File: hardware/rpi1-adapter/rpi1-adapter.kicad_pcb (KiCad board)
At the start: 2 copper layers, 98 x 68 mm, 29 parts, among them P1 I2C, P2 CONN_02X13, P3 UART, P4 CONN_01X08, P5 relays, P6 12V, P7 CONN_01X08, P8 CONN_01X08, U1 OPTO-TRANSISTOR-4, U2 OPTO-TRANSISTOR-4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

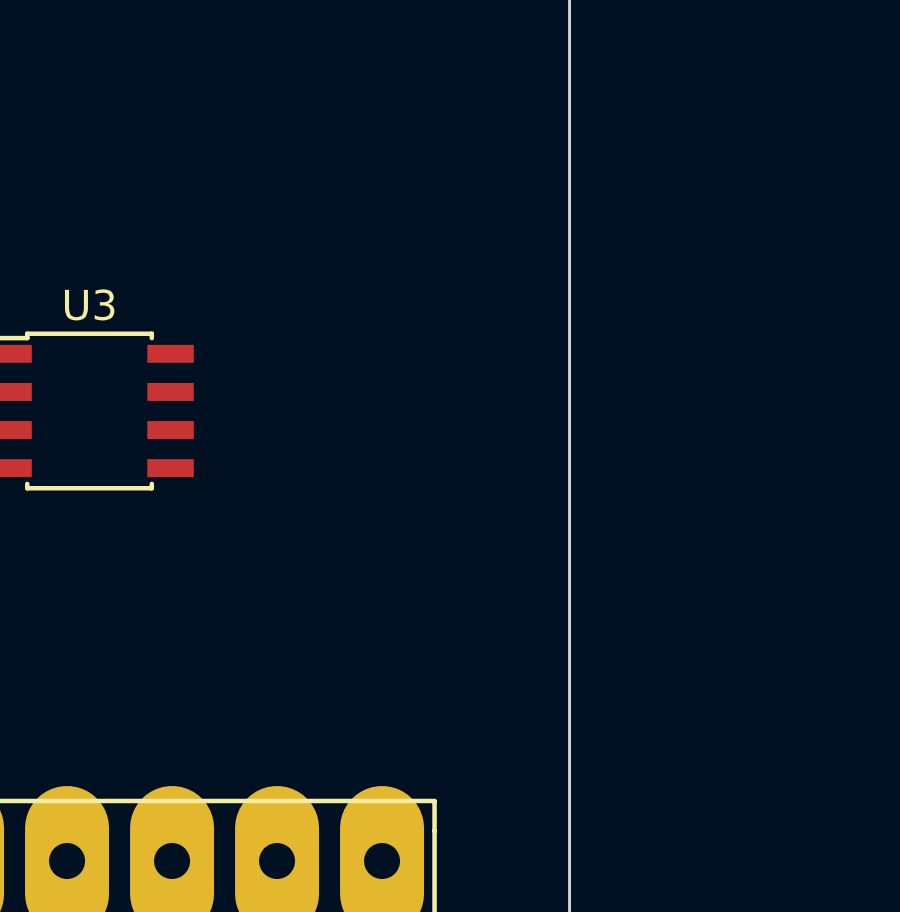
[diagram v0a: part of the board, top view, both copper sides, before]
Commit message: o Add dual P-mosfet to be used.
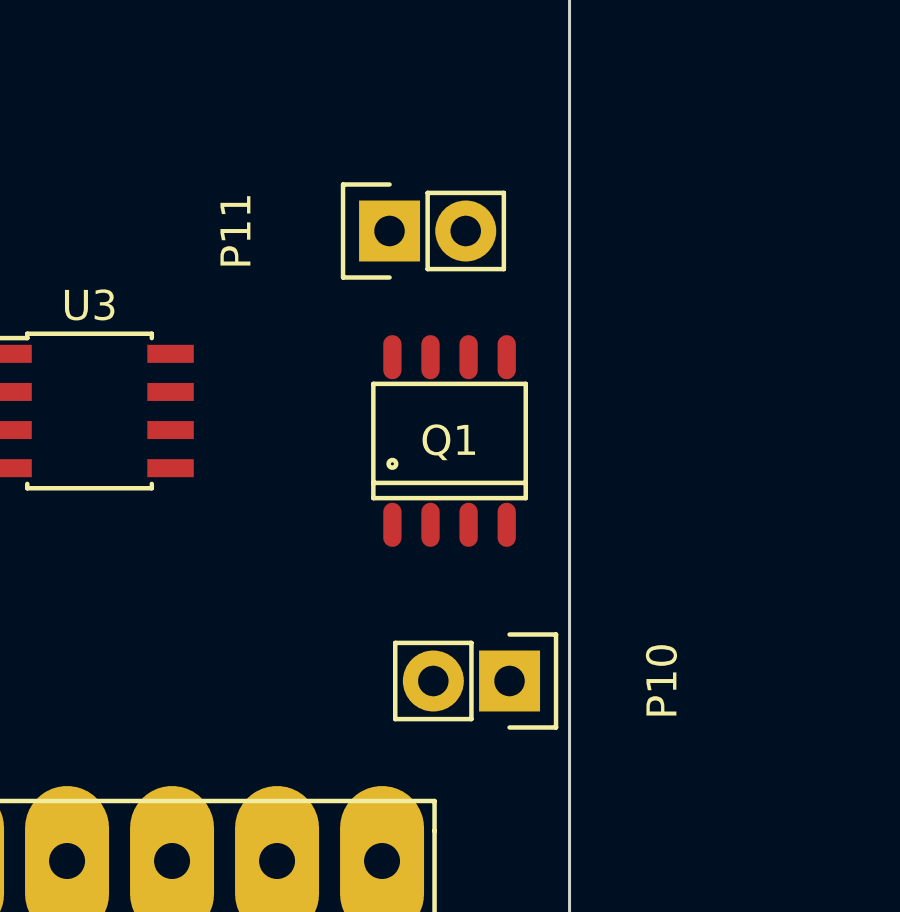
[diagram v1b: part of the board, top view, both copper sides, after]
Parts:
- added P10: CONN_01X02, Pin_Headers:Pin_Header_Straight_1x02, F.Cu at (146.0, 74.0)
- added P11: CONN_01X02, Pin_Headers:Pin_Header_Straight_1x02, F.Cu at (142.0, 59.0)
- added Q1: IRF9362PbF, SO-8, F.Cu at (144.0, 66.0)
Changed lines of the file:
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@@
 (kicad_pcb (version 4) (host pcbnew "(after 2015-may-25 BZR unknown)-product")
   (general
-    (links 96)
-    (no_connects 96)
-    (area 49.949999 21.949999 185.960003 90.050001)
+    (links 104)
+    (no_connects 104)
+    (area 49.949999 21.949999 148.050001 90.050001)
     (thickness 1.6)
     (drawings 4)
     (tracks 0)
     (zones 0)
-    (modules 29)
-    (nets 40)
+    (modules 32)
+    (nets 44)
   )
   (page A4)
@@
   (net 38 "Net-(C1-Pad1)")
   (net 39 "Net-(R10-Pad1)")
+  (net 40 "Net-(P11-Pad1)")
+  (net 41 "Net-(P10-Pad2)")
+  (net 42 "Net-(P11-Pad2)")
+  (net 43 "Net-(P10-Pad1)")
   (net_class Default "This is the default net class."
     (clearance 0.2)
@@
     (add_net "Net-(P1-Pad1)")
     (add_net "Net-(P1-Pad2)")
+    (add_net "Net-(P10-Pad1)")
+    (add_net "Net-(P10-Pad2)")
+    (add_net "Net-(P11-Pad1)")
+    (add_net "Net-(P11-Pad2)")
     (add_net "Net-(P2-Pad10)")
     (add_net "Net-(P2-Pad8)")
@@
     (pad 4 thru_hole oval (at -1.75 0) (size 2.8 5) (drill 1.2) (layers *.Cu *.Mask F.SilkS))
   )
+  (module SO-8 (layer F.Cu)
+    (at 144 66)
+    (descr "SO-8 Surface Mount Small Outline 150mil 8pin Package")
+    (tags "Power Integrations D Package")
+    (fp_text reference Q1 (at 0 0) (layer F.SilkS)
+      (effects (font (size 1 1) (thickness 0.15)))
+    )
+    (fp_text value IRF9362PbF (at 0 0) (layer F.Fab)
+      (effects (font (size 1 1) (thickness 0.15)))
+    )
+    (fp_circle (center -1.905 0.762) (end -1.778 0.762) (layer F.SilkS) (width 0.15))
+    (fp_line (start -2.54 1.397) (end 2.54 1.397) (layer F.SilkS) (width 0.15))
+    (fp_line (start -2.54 -1.905) (end 2.54 -1.905) (layer F.SilkS) (width 0.15))
+    (fp_line (start -2.54 1.905) (end 2.54 1.905) (layer F.SilkS) (width 0.15))
+    (fp_line (start -2.54 1.905) (end -2.54 -1.905) (layer F.SilkS) (width 0.15))
+    (fp_line (start 2.54 1.905) (end 2.54 -1.905) (layer F.SilkS) (width 0.15))
+    (pad 1 smd oval (at -1.905 2.794) (size 0.6096 1.4732) (layers F.Cu F.Paste F.Mask)
+      (net 35 +12V))
+    (pad 2 smd oval (at -0.635 2.794) (size 0.6096 1.4732) (layers F.Cu F.Paste F.Mask)
+      (net 41 "Net-(P10-Pad2)"))
+    (pad 3 smd oval (at 0.635 2.794) (size 0.6096 1.4732) (layers F.Cu F.Paste F.Mask)
+      (net 35 +12V))
+    (pad 4 smd oval (at 1.905 2.794) (size 0.6096 1.4732) (layers F.Cu F.Paste F.Mask)
+      (net 43 "Net-(P10-Pad1)"))
+    (pad 5 smd oval (at 1.905 -2.794) (size 0.6096 1.4732) (layers F.Cu F.Paste F.Mask)
+      (net 42 "Net-(P11-Pad2)"))
+    (pad 6 smd oval (at 0.635 -2.794) (size 0.6096 1.4732) (layers F.Cu F.Paste F.Mask)
+      (net 42 "Net-(P11-Pad2)"))
+    (pad 7 smd oval (at -0.635 -2.794) (size 0.6096 1.4732) (layers F.Cu F.Paste F.Mask)
+      (net 40 "Net-(P11-Pad1)"))
+    (pad 8 smd oval (at -1.905 -2.794) (size 0.6096 1.4732) (layers F.Cu F.Paste F.Mask)
+      (net 40 "Net-(P11-Pad1)"))
+  )
+  (module Pin_Headers:Pin_Header_Straight_1x02 (layer F.Cu)
+    (at 146 74 270)
+    (descr "Through hole pin header")
+    (tags "pin header")
+    (fp_text reference P10 (at 0 -5.1 270) (layer F.SilkS)
+      (effects (font (size 1 1) (thickness 0.15)))
+    )
+    (fp_text value CONN_01X02 (at 0 -3.1 270) (layer F.Fab)
+      (effects (font (size 1 1) (thickness 0.15)))
+    )
+    (fp_line (start 1.27 1.27) (end 1.27 3.81) (layer F.SilkS) (width 0.15))
+    (fp_line (start 1.55 -1.55) (end 1.55 0) (layer F.SilkS) (width 0.15))
+    (fp_line (start -1.75 -1.75) (end -1.75 4.3) (layer F.CrtYd) (width 0.05))
+    (fp_line (start 1.75 -1.75) (end 1.75 4.3) (layer F.CrtYd) (width 0.05))
+    (fp_line (start -1.75 -1.75) (end 1.75 -1.75) (layer F.CrtYd) (width 0.05))
+    (fp_line (start -1.75 4.3) (end 1.75 4.3) (layer F.CrtYd) (width 0.05))
+    (fp_line (start 1.27 1.27) (end -1.27 1.27) (layer F.SilkS) (width 0.15))
+    (fp_line (start -1.55 0) (end -1.55 -1.55) (layer F.SilkS) (width 0.15))
+    (fp_line (start -1.55 -1.55) (end 1.55 -1.55) (layer F.SilkS) (width 0.15))
+    (fp_line (start -1.27 1.27) (end -1.27 3.81) (layer F.SilkS) (width 0.15))
+    (fp_line (start -1.27 3.81) (end 1.27 3.81) (layer F.SilkS) (width 0.15))
+    (pad 1 thru_hole rect (at 0 0 270) (size 2.032 2.032) (drill 1.016) (layers *.Cu *.Mask F.SilkS)
+      (net 43 "Net-(P10-Pad1)"))
+    (pad 2 thru_hole oval (at 0 2.54 270) (size 2.032 2.032) (drill 1.016) (layers *.Cu *.Mask F.SilkS)
+      (net 41 "Net-(P10-Pad2)"))
+    (model Pin_Headers.3dshapes/Pin_Header_Straight_1x02.wrl
+      (at (xyz 0 -0.05 0))
+      (scale (xyz 1 1 1))
+      (rotate (xyz 0 0 90))
+    )
+  )
+  (module Pin_Headers:Pin_Header_Straight_1x02 (layer F.Cu)
+    (at 142 59 90)
+    (descr "Through hole pin header")
+    (tags "pin header")
+    (fp_text reference P11 (at 0 -5.1 90) (layer F.SilkS)
+      (effects (font (size 1 1) (thickness 0.15)))
+    )
+    (fp_text value CONN_01X02 (at 0 -3.1 90) (layer F.Fab)
+      (effects (font (size 1 1) (thickness 0.15)))
+    )
+    (fp_line (start 1.27 1.27) (end 1.27 3.81) (layer F.SilkS) (width 0.15))
+    (fp_line (start 1.55 -1.55) (end 1.55 0) (layer F.SilkS) (width 0.15))
+    (fp_line (start -1.75 -1.75) (end -1.75 4.3) (layer F.CrtYd) (width 0.05))
+    (fp_line (start 1.75 -1.75) (end 1.75 4.3) (layer F.CrtYd) (width 0.05))
+    (fp_line (start -1.75 -1.75) (end 1.75 -1.75) (layer F.CrtYd) (width 0.05))
+    (fp_line (start -1.75 4.3) (end 1.75 4.3) (layer F.CrtYd) (width 0.05))
+    (fp_line (start 1.27 1.27) (end -1.27 1.27) (layer F.SilkS) (width 0.15))
+    (fp_line (start -1.55 0) (end -1.55 -1.55) (layer F.SilkS) (width 0.15))
+    (fp_line (start -1.55 -1.55) (end 1.55 -1.55) (layer F.SilkS) (width 0.15))
+    (fp_line (start -1.27 1.27) (end -1.27 3.81) (layer F.SilkS) (width 0.15))
+    (fp_line (start -1.27 3.81) (end 1.27 3.81) (layer F.SilkS) (width 0.15))
+    (pad 1 thru_hole rect (at 0 0 90) (size 2.032 2.032) (drill 1.016) (layers *.Cu *.Mask F.SilkS)
+      (net 40 "Net-(P11-Pad1)"))
+    (pad 2 thru_hole oval (at 0 2.54 90) (size 2.032 2.032) (drill 1.016) (layers *.Cu *.Mask F.SilkS)
+      (net 42 "Net-(P11-Pad2)"))
+    (model Pin_Headers.3dshapes/Pin_Header_Straight_1x02.wrl
+      (at (xyz 0 -0.05 0))
+      (scale (xyz 1 1 1))
+      (rotate (xyz 0 0 90))
+    )
+  )
   (gr_line (start 50 22) (end 50 90) (angle 90) (layer Edge.Cuts) (width 0.1))

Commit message: o work in progress..
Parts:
- removed P10, P11: CONN_01X02, Pin_Headers:Pin_Header_Straight_1x02
- removed P5: relays, Pin_Headers:Pin_Header_Straight_2x06
- added D10: Led_Small, LEDs:LED-0805, F.Cu at (138.0, 102.7)
- added D11: Led_Small, LEDs:LED-0805, F.Cu at (91.4, 67.3)
- added D2: D, Diodes_ThroughHole:Diode_DO-35_SOD27_Horizontal_RM10, F.Cu at (106.5, 113.2)
- added D3: D, Diodes_ThroughHole:Diode_DO-35_SOD27_Horizontal_RM10, F.Cu at (106.5, 105.0)
- added D4: Led_Small, LEDs:LED-0805, F.Cu at (109.5, 119.1)
- added D5: Led_Small, LEDs:LED-0805, F.Cu at (121.7, 110.9)
- added D6: Led_Small, LEDs:LED-0805, F.Cu at (97.8, 73.7)
- added D7: Led_Small, LEDs:LED-0805, F.Cu at (109.5, 123.7)
- added D8: Led_Small, LEDs:LED-0805, F.Cu at (117.6, 119.1)
- added D9: Led_Small, LEDs:LED-0805, F.Cu at (129.8, 110.9)
- added Q2: IRF9362PbF, Power_Integrations:SO-8, F.Cu at (137.2, 71.1)
- added R12: 180, Resistors_SMD:R_0805_HandSoldering, F.Cu at (129.5, 122.7)
- added R13: 180, Resistors_SMD:R_0805_HandSoldering, F.Cu at (141.8, 109.9)
- added R14: 180, Resistors_SMD:R_0805_HandSoldering, F.Cu at (149.9, 103.6)
- added R15: 180, Resistors_SMD:R_0805_HandSoldering, F.Cu at (136.5, 108.2)
- added R16: R, Resistors_SMD:R_0805_HandSoldering, F.Cu at (147.0, 109.9)
- added R17: R, Resistors_SMD:R_0805_HandSoldering, F.Cu at (141.8, 116.2)
- added R18: R, Resistors_SMD:R_0805_HandSoldering, F.Cu at (147.0, 116.2)
- added R19: R, Resistors_SMD:R_0805_HandSoldering, F.Cu at (139.8, 122.5)
- added U4: OPTO-TRANSISTOR-4, Housings_DIP:DIP-16_W7.62mm_LongPads, F.Cu at (138.4, 55.9)
- P4: value CONN_01X08 -> Sensors 1
- P7: value CONN_01X08 -> Sensors 2
- P8: value CONN_01X08 -> 12V actor outputs
- Q1: footprint SO-8 -> Power_Integrations:SO-8
- R1, R2, R3, R4, R5, R6, R7, R8: value R -> 1k2; footprint Resistors_ThroughHole:Resistor_Vertical_RM5mm -> Resistors_SMD:R_0805_HandSoldering
- moved C5 106.1 mm to (129.2, 116.4)
- moved C2 97.5 mm to (124.2, 116.4)
- moved R9 97.1 mm to (124.3, 122.7)
- moved L1 95.8 mm to (121.7, 104.4)
- moved C1 93.1 mm to (134.7, 120.8)
- moved R11 86.5 mm to (136.5, 114.5)
- moved R10 78.8 mm to (144.7, 103.6)
- moved U1 28.8 mm to (91.4, 63.5)
- moved U3 24.0 mm to (115.0, 48.0)
- moved U2 21.9 mm to (63.5, 63.5)
- moved Q1 20.2 mm to (124.5, 71.1), turned to 180 degrees
- moved R8 13.0 mm to (88.9, 73.7)
- moved R5 12.9 mm to (109.0, 70.0)
- moved R6 11.5 mm to (102.0, 70.0)
- moved R7 10.3 mm to (95.0, 70.0)
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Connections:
- C2 pad 2: +12V -> Net-(C2-Pad2)
- C3 pad 1: +12V -> Net-(C2-Pad2)
- P6 pad 2: +12V -> PowerIn
- P8 pad 2: (no net) -> Net-(P8-Pad2)
- P8 pad 4: (no net) -> Net-(P8-Pad4)
- P8 pad 6: (no net) -> Net-(P8-Pad6)
- P8 pad 8: (no net) -> Net-(P8-Pad8)
- Q1 pad 5: Net-(P11-Pad2) -> Net-(P8-Pad2)
- Q1 pad 6: Net-(P11-Pad2) -> Net-(P8-Pad2)
- Q1 pad 7: Net-(P11-Pad1) -> Net-(P8-Pad4)
- Q1 pad 8: Net-(P11-Pad1) -> Net-(P8-Pad4)
- R1 pad 1: +5V -> +12V
- R1 pad 2: Net-(R1-Pad2) -> Net-(D8-Pad2)
- R2 pad 1: +5V -> +12V
- R2 pad 2: Net-(R2-Pad2) -> Net-(D4-Pad2)
- R3 pad 1: +5V -> +12V
- R3 pad 2: Net-(R3-Pad2) -> Net-(D5-Pad2)
- R4 pad 1: +5V -> +12V
- R4 pad 2: Net-(R4-Pad2) -> Net-(D6-Pad2)
- R5 pad 1: +5V -> +12V
- R5 pad 2: Net-(R5-Pad2) -> Net-(D7-Pad2)
- R6 pad 1: +5V -> +12V
- R6 pad 2: Net-(R6-Pad2) -> Net-(D9-Pad2)
- R7 pad 1: +5V -> +12V
- R7 pad 2: Net-(R7-Pad2) -> Net-(D10-Pad2)
- R8 pad 1: +5V -> +12V
- R8 pad 2: Net-(R8-Pad2) -> Net-(D11-Pad2)
- R9 pad 2: +12V -> Net-(C2-Pad2)
- U1 pad 1: Net-(R5-Pad2) -> Net-(D11-Pad1)
- U1 pad 10: in-4 -> in-17
- U1 pad 12: in-21 -> in-22
- U1 pad 14: in-22 -> in-21
- U1 pad 16: in-17 -> in-4
- U1 pad 2: Net-(P7-Pad8) -> Net-(P7-Pad2)
- U1 pad 3: Net-(R6-Pad2) -> Net-(D10-Pad1)
- U1 pad 4: Net-(P7-Pad6) -> Net-(P7-Pad4)
- U1 pad 5: Net-(R7-Pad2) -> Net-(D9-Pad1)
- U1 pad 6: Net-(P7-Pad4) -> Net-(P7-Pad6)
- U1 pad 7: Net-(R8-Pad2) -> (no net)
- U1 pad 8: Net-(P7-Pad2) -> Net-(P7-Pad8)
- U2 pad 1: Net-(R1-Pad2) -> Net-(D6-Pad1)
- U2 pad 10: in-24 -> in-11
- U2 pad 12: in-23 -> in-18
- U2 pad 14: in-18 -> in-23
- U2 pad 16: in-11 -> in-24
- U2 pad 2: Net-(P4-Pad8) -> Net-(P4-Pad2)
- U2 pad 3: Net-(R2-Pad2) -> Net-(D5-Pad1)
- U2 pad 4: Net-(P4-Pad6) -> Net-(P4-Pad4)
- U2 pad 5: Net-(R3-Pad2) -> Net-(D4-Pad1)
- U2 pad 6: Net-(P4-Pad4) -> Net-(P4-Pad6)
- U2 pad 7: Net-(R4-Pad2) -> Net-(D8-Pad1)
- U2 pad 8: Net-(P4-Pad2) -> Net-(P4-Pad8)
- U3 pad 6: +12V -> Net-(C2-Pad2)

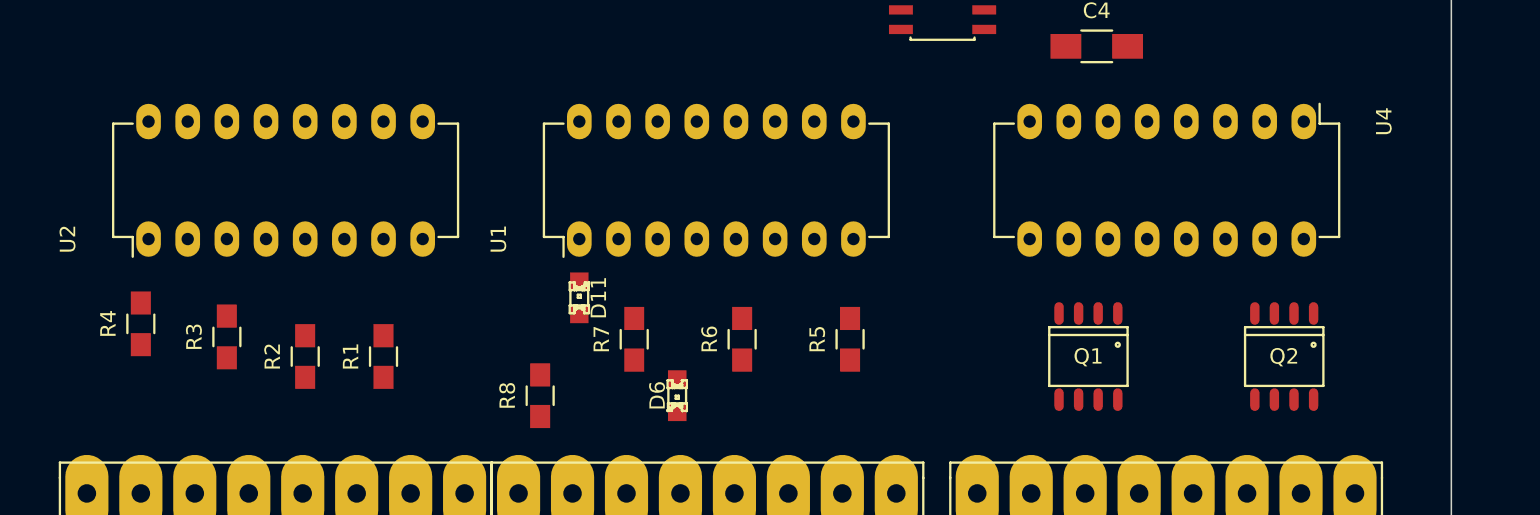
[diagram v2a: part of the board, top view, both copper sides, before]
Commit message: o Add free-wheel diodes.
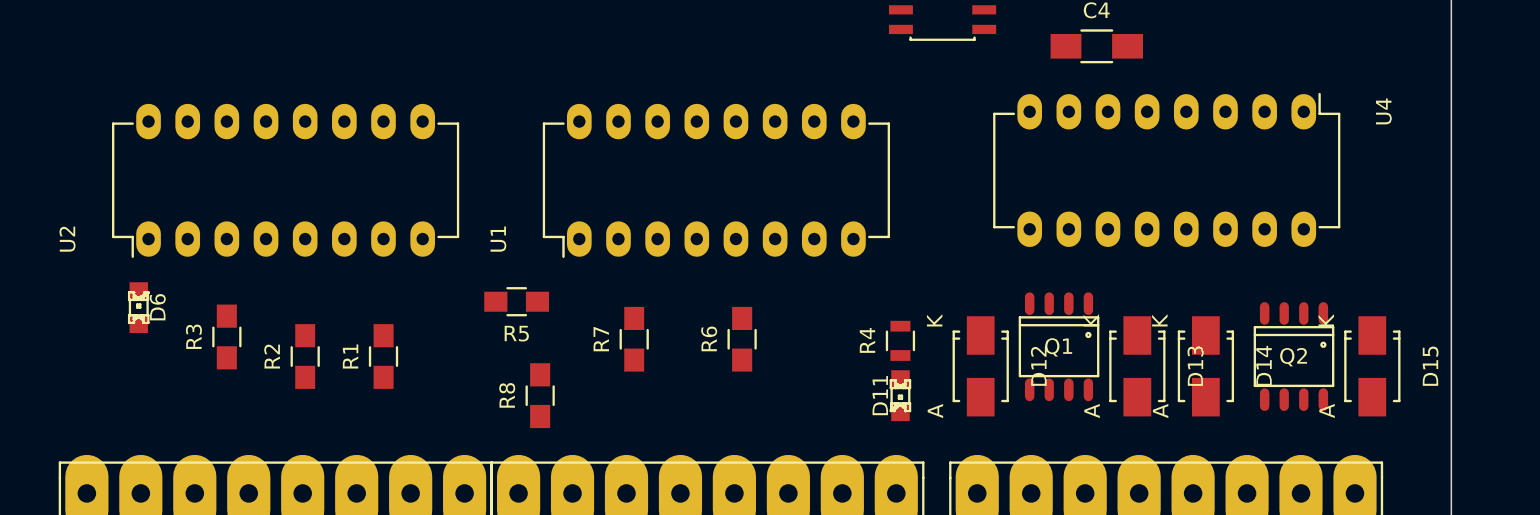
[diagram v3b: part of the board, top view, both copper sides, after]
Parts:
- added D12: S1B, Diodes_SMD:Diode-SMA_Standard, F.Cu at (117.5, 71.8)
- added D13: S1B, Diodes_SMD:Diode-SMA_Standard, F.Cu at (127.6, 71.8)
- added D14: S1B, Diodes_SMD:Diode-SMA_Standard, F.Cu at (132.1, 71.8)
- added D15: S1B, Diodes_SMD:Diode-SMA_Standard, F.Cu at (142.9, 71.8)
- R4: footprint Resistors_SMD:R_0805_HandSoldering -> Resistors_SMD:R_0805
- moved R4 49.3 mm to (112.3, 70.1)
- moved D6 35.4 mm to (62.9, 67.9), turned to 270 degrees
- moved D11 21.8 mm to (112.3, 73.7), turned to 90 degrees
- moved R5 21.8 mm to (87.4, 67.6), turned to 180 degrees
- moved Q1 2.01 mm to (122.6, 70.5)
- moved U4 0.64 mm to (138.4, 55.2)
- moved Q2 0.63 mm to (137.8, 71.1)
